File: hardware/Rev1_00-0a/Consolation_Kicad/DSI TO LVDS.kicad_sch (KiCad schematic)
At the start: 27 parts, among them Q10 SSM3K56FS,LF, Q11 SSM3K56FS,LF, U15 SN65DSI84ZXHR, U16 SN74LVC1G125DBVR

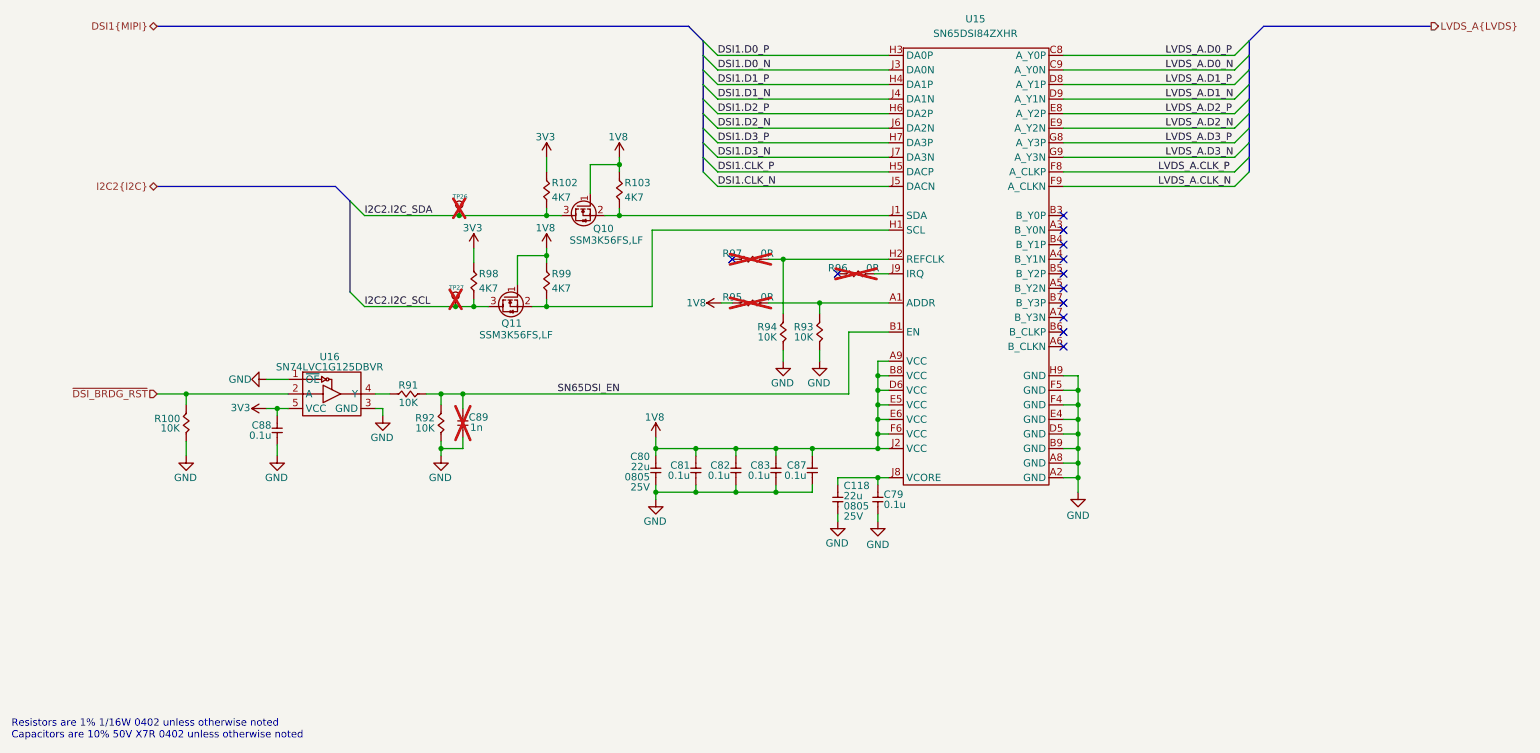
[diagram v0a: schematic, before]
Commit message: Removed unnecessary functions (USB2 mux, CapTouch) Adjusted 220uF alum capacitor for codec (slimmer version)
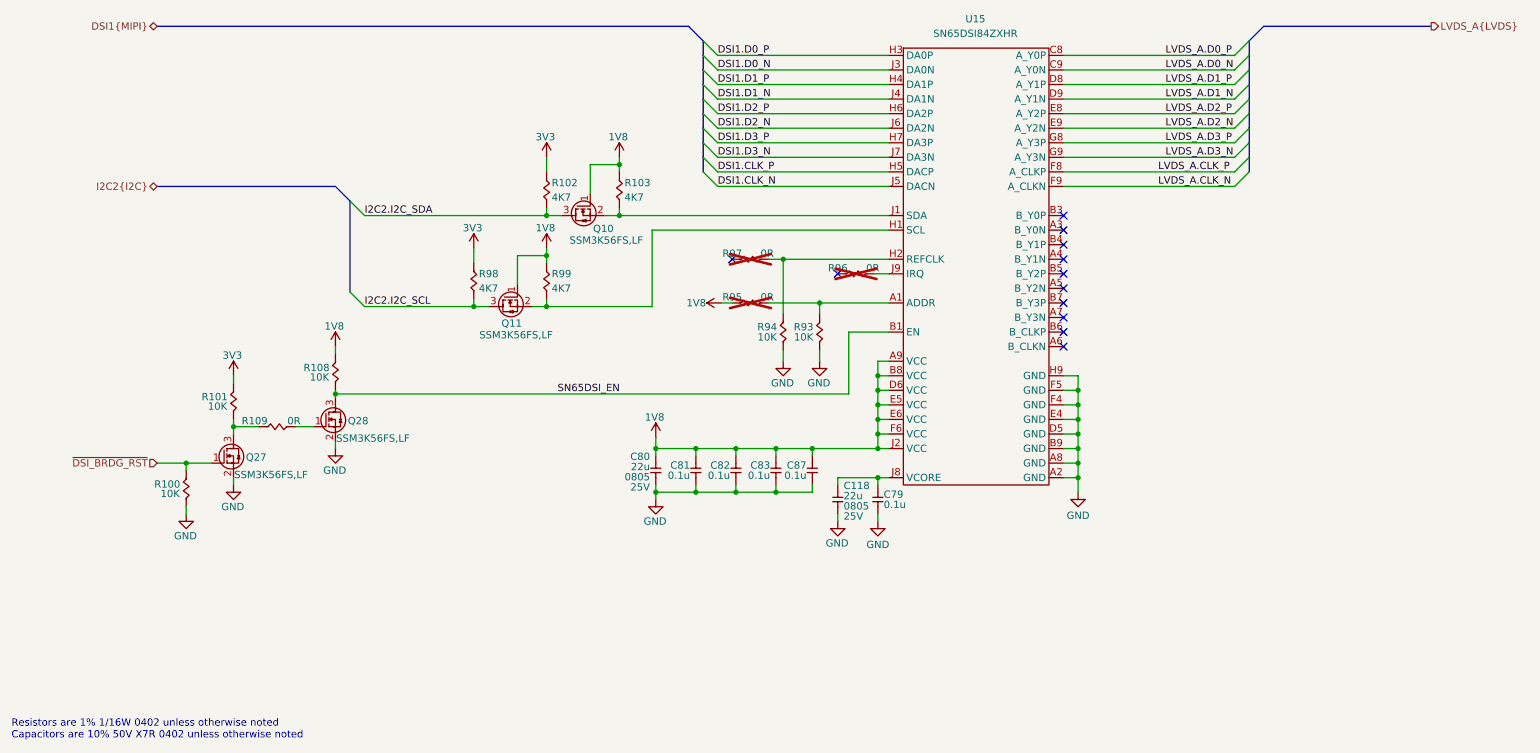
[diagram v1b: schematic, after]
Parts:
- removed C88: 0.1u, footprint:CAP_NONPOL_0402, symbol KicadCompDb:Capacitors/CAP_CER_SMT_00001
- removed C89: 1n, footprint:CAP_NONPOL_0402, symbol KicadCompDb:Capacitors/CAP_CER_SMT_00005
- removed R91, R92: 10K, footprint:RES_0402, symbol KicadCompDb:Resistors/RES_SMT_00013
- removed TP26, TP27: 28 mils, footprint:SMT_TP_28_MILS, symbol KicadCompDb:Test Point/TP_00001
- removed U16: SN74LVC1G125DBVR, footprint:SOT-23-5, symbol KicadCompDb:Logic/LOGIC_00001
- added Q27, Q28: SSM3K56FS,LF, footprint:SC-75, symbol KicadCompDb:Mosfet/MOSFET_00002
- added R101, R108: 10K, footprint:RES_0402, symbol KicadCompDb:Resistors/RES_SMT_00013
- added R109: 0R, footprint:RES_0402, symbol KicadCompDb:Resistors/RES_SMT_00001
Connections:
- net 1V8: now also R108.2
- net 3V3: now also R101.2
- net GND: now also Q27.2 (S), Q28.2 (S)
- net SN65DSI_EN: now also Q28.3 (D), R108.1
- net ~{DSI_BRDG_RST}: now also Q27.1 (G)
- new net: Q27.3 (D), R101.1, R109.1
- new net: Q28.1 (G), R109.2
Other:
- moved on the sheet: R100

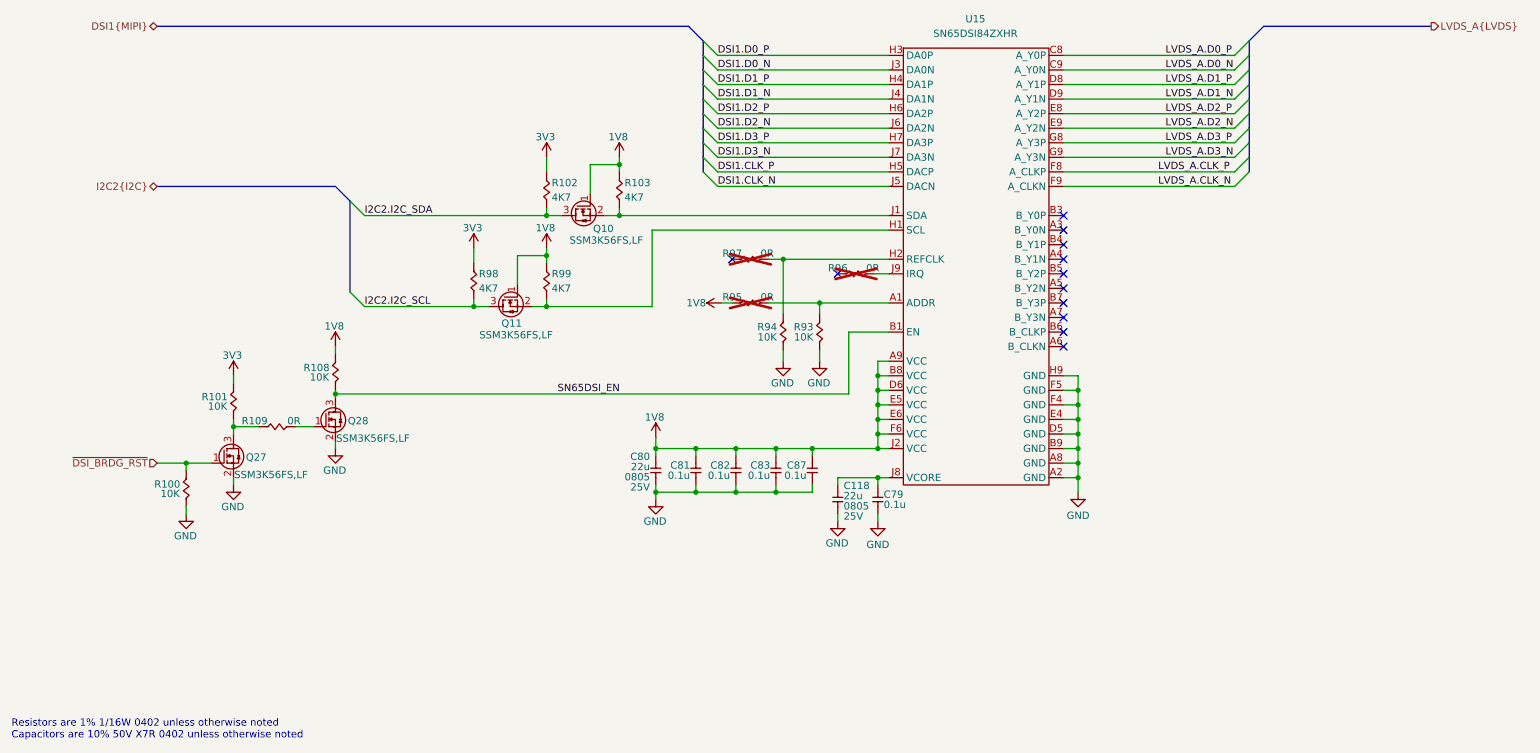
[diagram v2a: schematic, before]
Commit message: Continue preliminary placement To do : Power supplies + Type C charger
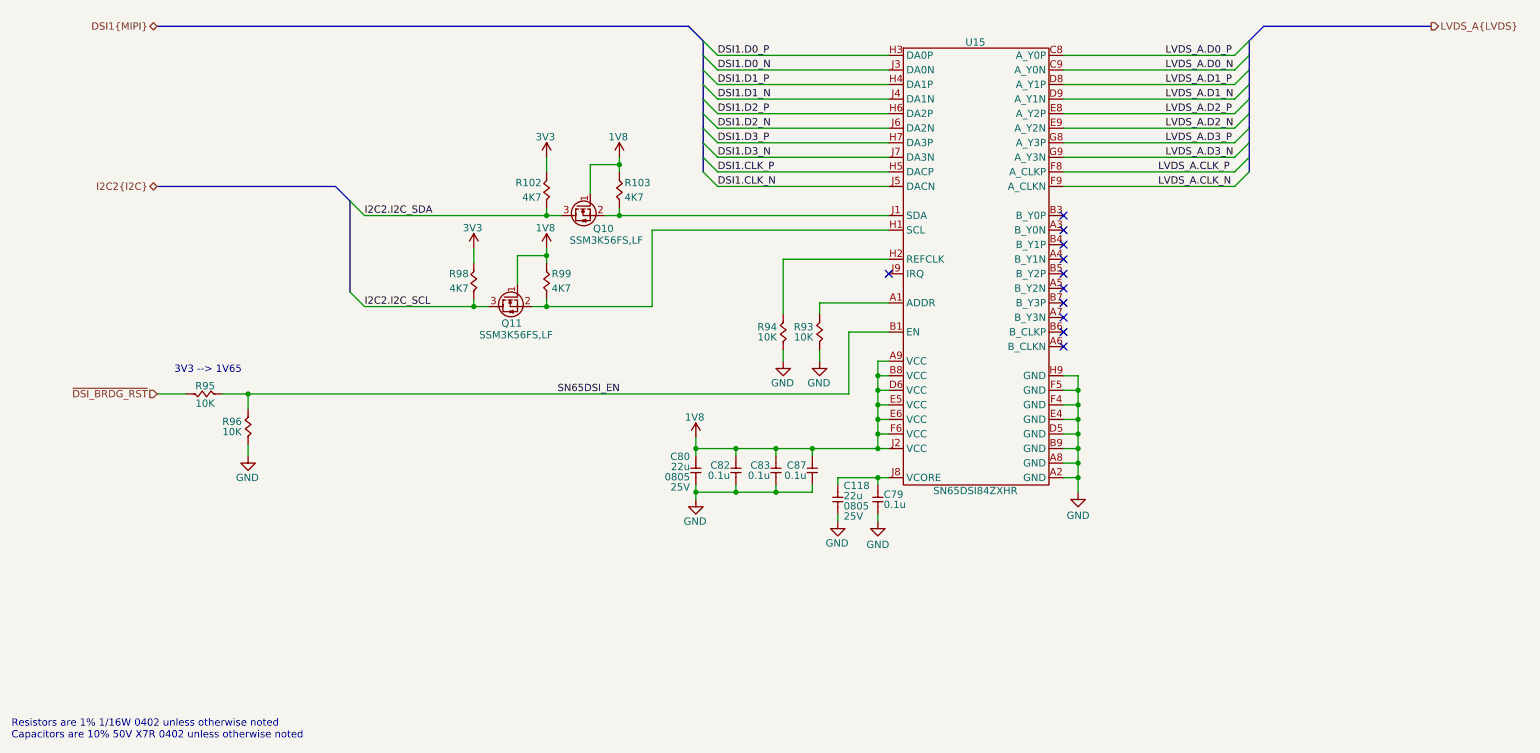
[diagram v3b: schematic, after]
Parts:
- removed C81: 0.1u, footprint:CAP_NONPOL_0402, symbol KicadCompDb:Capacitors/CAP_CER_SMT_00001
- removed Q27, Q28: SSM3K56FS,LF, footprint:SC-75, symbol KicadCompDb:Mosfet/MOSFET_00002
- removed R100, R101, R108: 10K, footprint:RES_0402, symbol KicadCompDb:Resistors/RES_SMT_00013
- removed R109, R95, R96, R97: 0R, footprint:RES_0402, symbol KicadCompDb:Resistors/RES_SMT_00001
- added R95, R96: 10K, footprint:RES_0402, symbol KicadCompDb:Resistors/RES_SMT_00013
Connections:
- net GND: now also R96.1
- net SN65DSI_EN: now also R95.1, R96.2
- net ~{DSI_BRDG_RST}: now also R95.2
- no-connect marks 12 -> 11
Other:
- note added: "3V3 --> 1V65"
- moved on the sheet: C80, R102, R98

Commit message: Preliminary placement done Add test points to PCB
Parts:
- added TP21, TP22: 75 mils, footprint:SMT_TP_75_MILS, symbol KicadCompDb:Test Point/TP_00004
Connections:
- net I2C2.I2C_SCL: now also TP22.1
- net I2C2.I2C_SDA: now also TP21.1

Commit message: Preliminary routing (DiffPairs, Power planes) in progress Slight changes to schematics to accommodate routing
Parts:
- removed C118: 22u, footprint:CAP_NONPOL_0805, symbol KicadCompDb:Capacitors/CAP_CER_SMT_00011
- added C48: 1u, footprint:CAP_NONPOL_0805, symbol KicadCompDb:Capacitors/CAP_CER_SMT_00002
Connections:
- net GND: now also C48.1
- net at C79.2, U15.J8 (VCORE): now also C48.2
